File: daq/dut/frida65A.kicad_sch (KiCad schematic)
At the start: 68 parts, among them J1 TP_PWR, J10 TP_LOGIC, J11 TP_OUT, J12 J_P, J16 J_N, J17 Molex_02x04_Mini-Fit_Jr, J2 CONN_IN_P, J3 CONN_IN_N, J4 TP_CFG, J5 CONN_CFG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

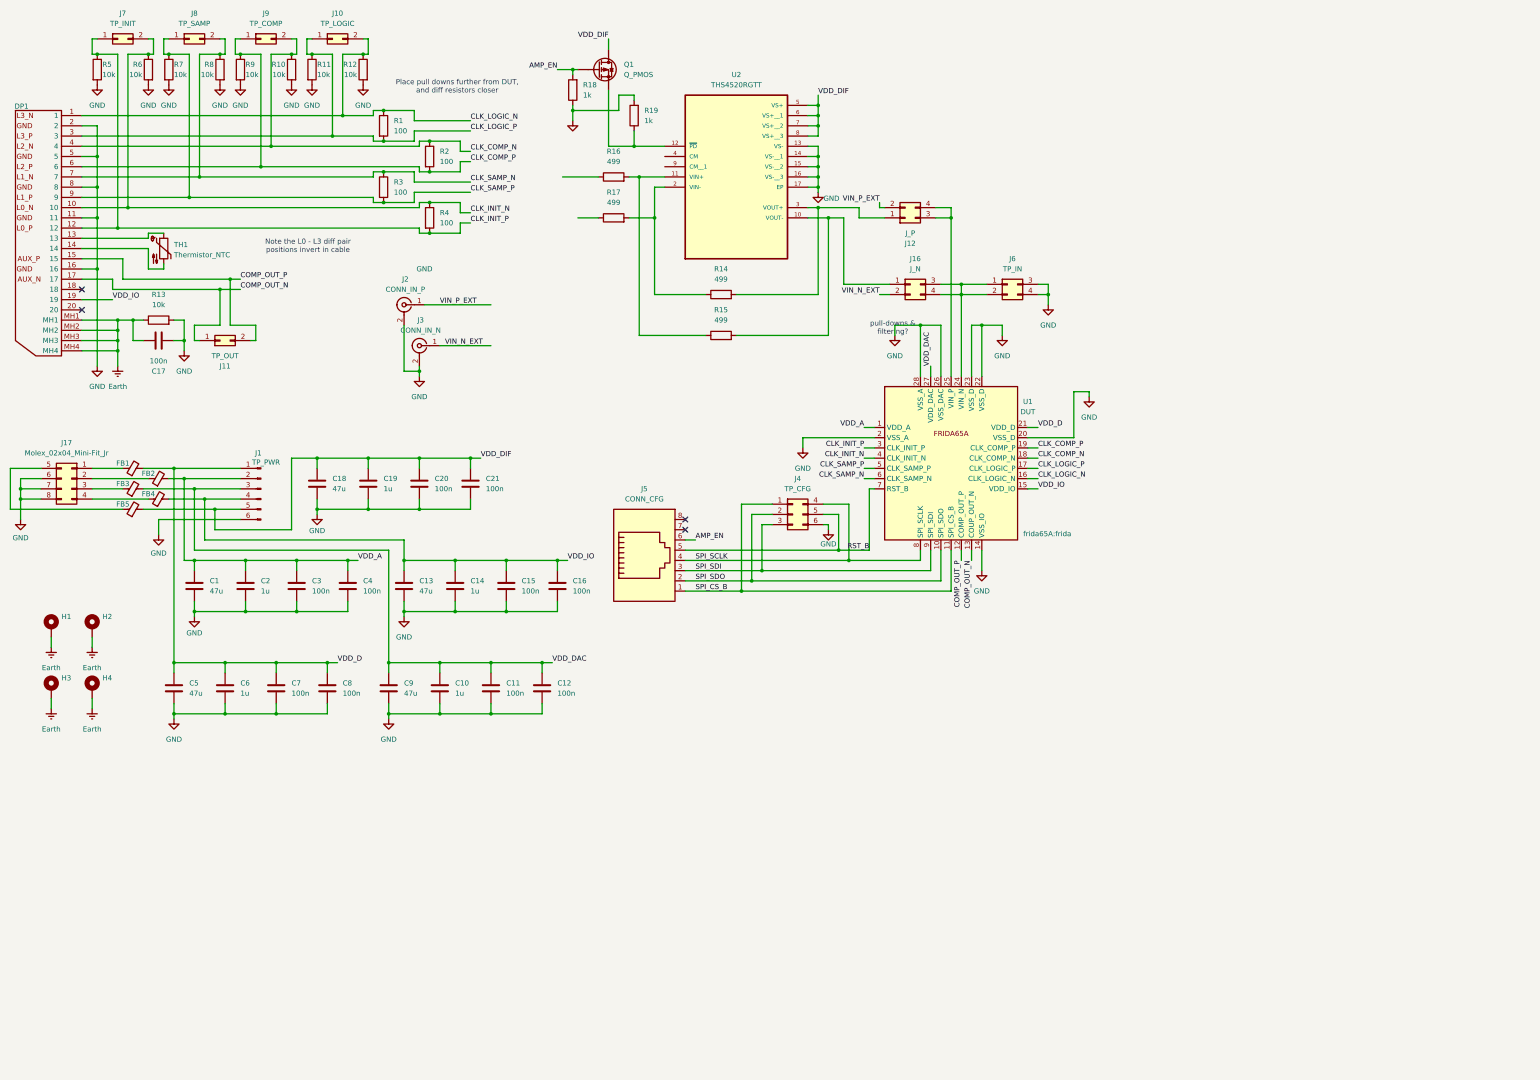
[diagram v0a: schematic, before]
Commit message: Update PCB symbols, footprints, and models. Start work on Spectre simulator montecarlo support.
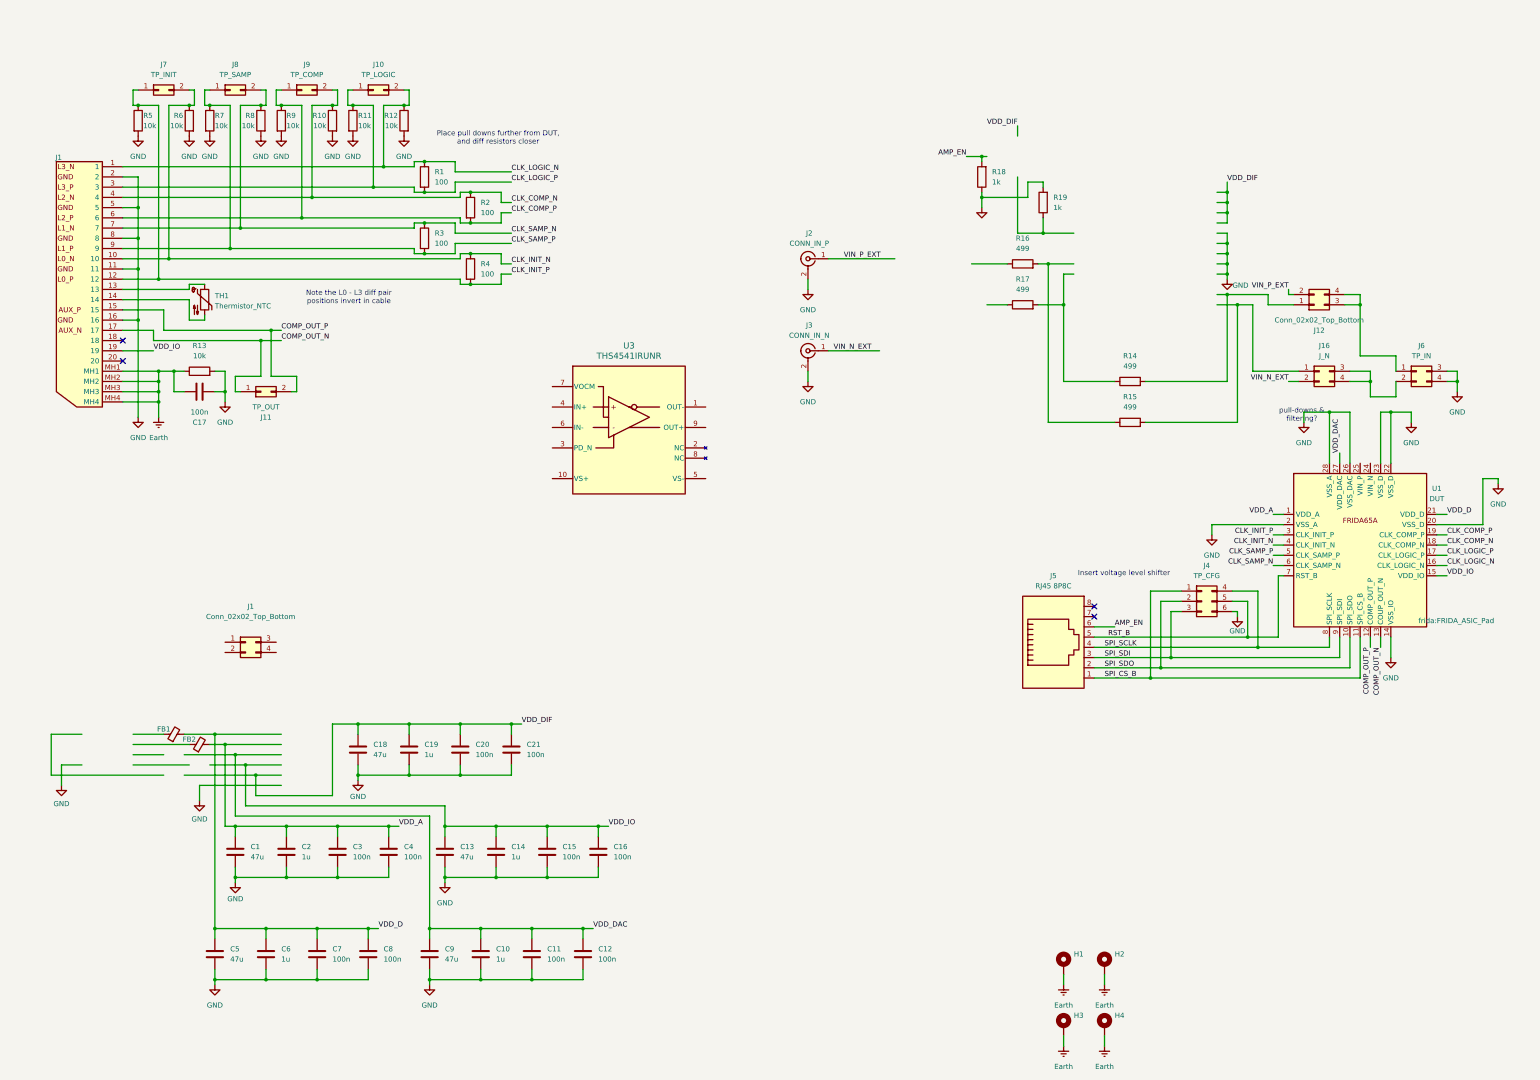
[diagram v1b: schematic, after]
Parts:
- removed DP1: DP, frida65A:displayport, symbol silab:DP Molex 47272-0024
- removed FB3, FB4, FB5: FerriteBead_Small, Resistor_SMD:R_0603_1608Metric, symbol Device:FerriteBead_Small
- removed J1: TP_PWR, frida65A:Molex_Mini-Fit_Jr_5569-08A1_2x04_P4.20mm_Horizontal, symbol Connector:Conn_01x06_Pin
- removed J17: Molex_02x04_Mini-Fit_Jr, Silab:Molex_Mini-Fit_Jr_02x04_horizontal, symbol frida:Molex_02x04_Mini-Fit_Jr
- removed Q1: Q_PMOS, symbol Device:Q_PMOS
- removed U2: THS4520RGTT, frida65A:QFN50P300X300X100-17N, symbol frida:THS4520RGTT
- added J1: Conn_02x02_Top_Bottom, Connector_PinHeader_2.54mm:PinHeader_2x02_P2.54mm_Vertical, symbol Connector_Generic:Conn_02x02_Top_Bottom
- added J1: DP, frida:Molex_DisplayPort_472720024, symbol frida:Molex_DisplayPort_472720024
- added U3: THS4541IRUNR, Package_DFN_QFN:Texas_RUN0010A_WQFN-10_2x2mm_P0.5mm, symbol frida:TI_DiffAmp_THS4541
- J12: value J_P -> Conn_02x02_Top_Bottom; footprint frida65A:Molex_Mini-Fit_Jr_5569-08A1_2x04_P4.20mm_Horizontal -> Connector_PinHeader_2.54mm:PinHeader_2x02_P2.54mm_Vertical
- J16: footprint frida65A:displayport -> frida:Molex_DisplayPort_472720024
- J5: value CONN_CFG -> RJ45 8P8C; footprint Connector_RJ:RJ45_Amphenol_54602-x08_Horizontal -> frida:Molex_RJ45_446200002; symbol frida:RJ45 -> Connector:RJ45
- U1: footprint frida65A:frida -> frida:FRIDA_ASIC_Pad; symbol frida:frida_pad -> frida:FRIDA_ASIC_Pad
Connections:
- net CLK_COMP_N: now also J1.4
- net CLK_COMP_P: now also J1.6
- net CLK_INIT_N: now also J1.10
- net CLK_INIT_P: now also J1.12
- net CLK_LOGIC_N: now also J1.1
- net CLK_LOGIC_P: now also J1.3
- net CLK_SAMP_N: now also J1.7
- net CLK_SAMP_P: now also J1.9
- net COMP_OUT_N: now also J1.17
- net COMP_OUT_P: now also J1.15
- net Earth: now also J1.MH1, J1.MH2, J1.MH3, J1.MH4
- net GND: now also J1.11, J1.16, J1.2, J1.5, J1.8
- net VDD_IO: now also J1.19
- net at J16.3 (Pin_3), J16.4 (Pin_4), J6.2 (Pin_2): no longer J6.1 (Pin_1), U1.24 (VIN_N)
- net at J12.3 (Pin_3), J12.4 (Pin_4): now also J6.1 (Pin_1); no longer U1.25 (VIN_P)
- net at TH1.1: now also J1.13
- net at TH1.2: now also J1.14
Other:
- note added: "Insert voltage level shifter"
- moved on the sheet: C1, C10, C11, C12, C13, C14, C15, C16, C17, C18, C19, C2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

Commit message: Update schematic with new arch, and remove 2.54mm testpoints
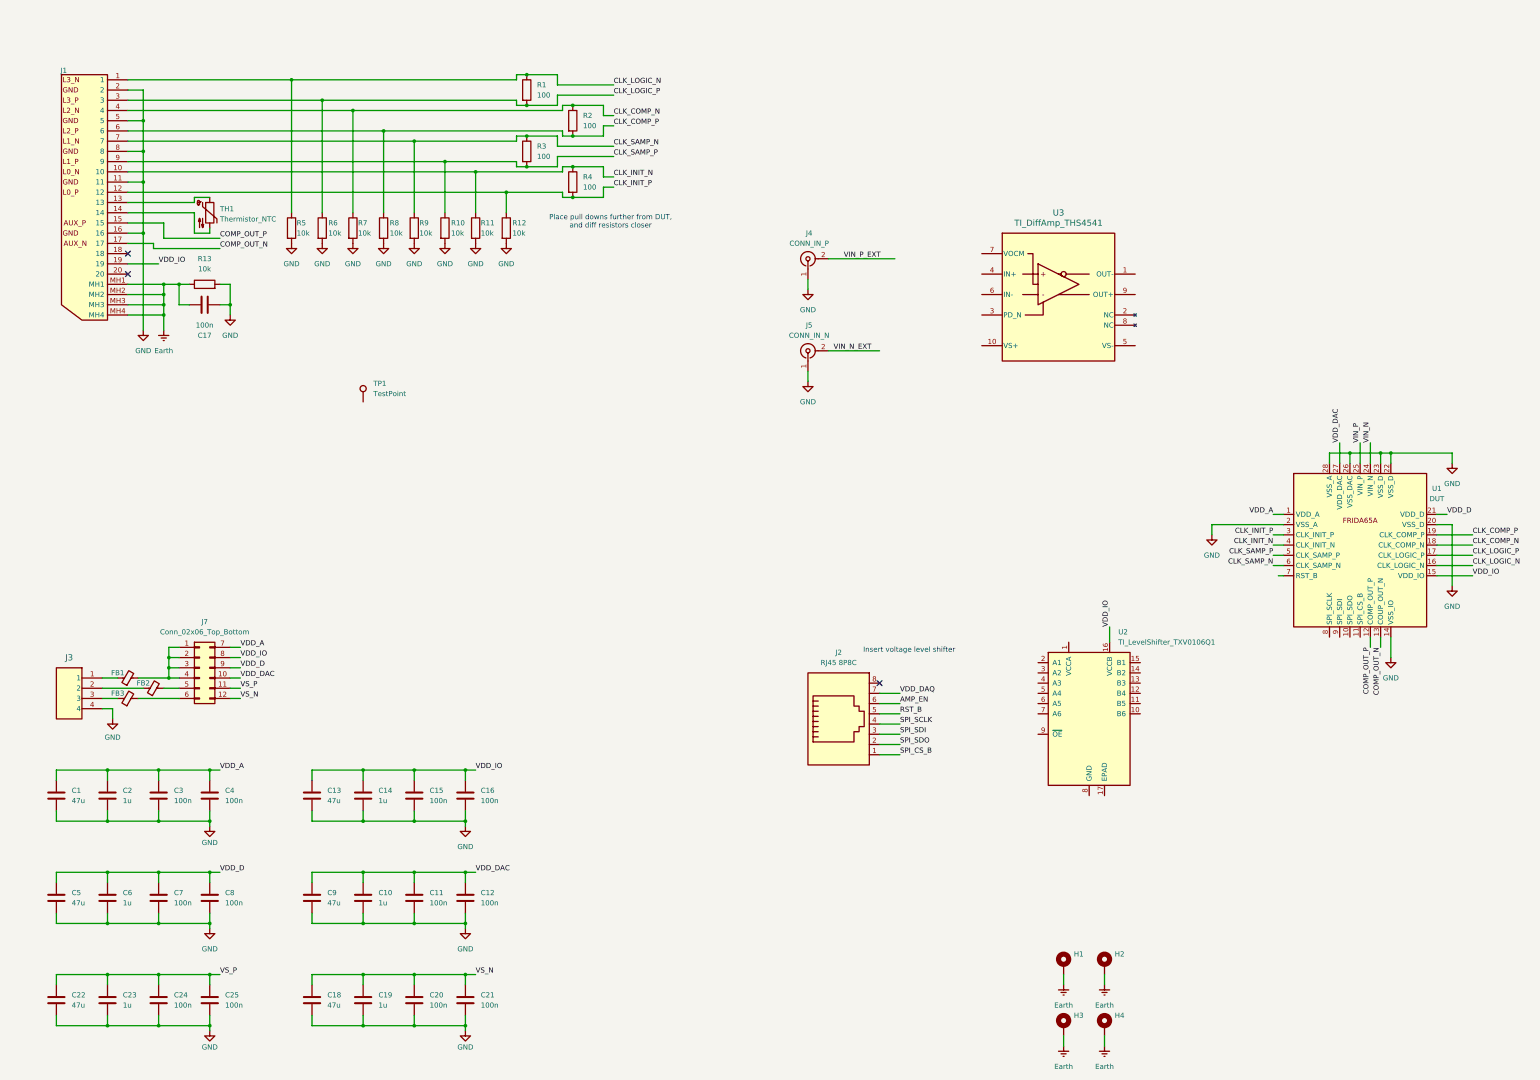
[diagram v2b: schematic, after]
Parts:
- removed J1, J12: Conn_02x02_Top_Bottom, Connector_PinHeader_2.54mm:PinHeader_2x02_P2.54mm_Vertical, symbol Connector_Generic:Conn_02x02_Top_Bottom
- removed J10: TP_LOGIC, Connector_PinHeader_2.54mm:PinHeader_2x01_P2.54mm_Vertical, symbol Connector_Generic:Conn_02x01
- removed J11: TP_OUT, Connector_PinHeader_2.54mm:PinHeader_2x01_P2.54mm_Vertical, symbol Connector_Generic:Conn_02x01
- removed J16: J_N, frida:Molex_DisplayPort_472720024, symbol Connector_Generic:Conn_02x02_Top_Bottom
- removed J4: TP_CFG, Connector_PinHeader_2.54mm:PinHeader_2x03_P2.54mm_Vertical, symbol Connector_Generic:Conn_02x03_Top_Bottom
- removed J6: TP_IN, Connector_PinHeader_2.54mm:PinHeader_2x02_P2.54mm_Vertical, symbol Connector_Generic:Conn_02x02_Top_Bottom
- removed J7: TP_INIT, Connector_PinHeader_2.54mm:PinHeader_2x01_P2.54mm_Vertical, symbol Connector_Generic:Conn_02x01
- removed J8: TP_SAMP, Connector_PinHeader_2.54mm:PinHeader_2x01_P2.54mm_Vertical, symbol Connector_Generic:Conn_02x01
- removed J9: TP_COMP, Connector_PinHeader_2.54mm:PinHeader_2x01_P2.54mm_Vertical, symbol Connector_Generic:Conn_02x01
- removed R14, R15, R16, R17: 499, Resistor_SMD:R_0603_1608Metric, symbol Device:R
- removed R18, R19: 1k, Resistor_SMD:R_0603_1608Metric, symbol Device:R
- added C22: 47u, Capacitor_SMD:C_0603_1608Metric, symbol Device:C
- added C23: 1u, Capacitor_SMD:C_0603_1608Metric, symbol Device:C
- added C24, C25: 100n, Capacitor_SMD:C_0603_1608Metric, symbol Device:C
- added FB3: FerriteBead_Small, Resistor_SMD:R_0603_1608Metric, symbol Device:FerriteBead_Small
- added J3: Molex_MiniFitJr_469990014, frida:Molex_MiniFitJr_469990014, symbol frida:Molex_MiniFitJr_469990014
- added J7: Conn_02x06_Top_Bottom, symbol Connector_Generic:Conn_02x06_Top_Bottom
- added TP1: TestPoint, TestPoint:TestPoint_Pad_D2.0mm, symbol Connector:TestPoint
- added U2: TI_LevelShifter_TXV0106Q1, Package_DFN_QFN:WQFN-16-1EP_4x4mm_P0.5mm_EP2.6x2.6mm, symbol frida:TI_LevelShifter_TXV0106Q1
- J4: renamed from J2; footprint Connector_Coaxial:SMA_Amphenol_901-143_Horizontal -> frida:Molex_SMA_733910070; symbol dmaps_components:Conn_LEMO -> frida:Molex_SMA_733910070
- J5: renamed from J3; footprint Connector_Coaxial:SMA_Amphenol_901-143_Horizontal -> frida:Molex_SMA_733910070; symbol dmaps_components:Conn_LEMO -> frida:Molex_SMA_733910070
- U3: value THS4541IRUNR -> TI_DiffAmp_THS4541; footprint Package_DFN_QFN:Texas_RUN0010A_WQFN-10_2x2mm_P0.5mm -> frida:TI_DiffAmp_THS4541
- renumbered J5 to J2
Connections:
- net CLK_COMP_N: now also R7.1; no longer R10.1
- net CLK_COMP_P: now also R8.1; no longer R9.1
- net CLK_INIT_N: now also R11.1; no longer R6.1
- net CLK_INIT_P: now also R12.1; no longer R5.1
- net CLK_LOGIC_N: now also R5.1; no longer R12.1
- net CLK_LOGIC_P: now also R6.1; no longer R11.1
- net CLK_SAMP_N: now also R9.1; no longer R8.1
- net CLK_SAMP_P: now also R10.1; no longer R7.1
- net GND: now also J4.1 (In), J5.1 (In), C22.2, C23.2, C24.2, C25.2, J3.4; no longer J4.2 (Ext), J5.2 (Ext)
- net RST_B: no longer U1.7 (RST_B)
- net SPI_CS_B: no longer U1.11 (SPI_CS_B)
- net SPI_SCLK: no longer U1.8 (SPI_SCLK)
- net SPI_SDI: no longer U1.9 (SPI_SDI)
- net SPI_SDO: no longer U1.10 (SPI_SDO)
- net VDD_A: now also J7.7 (Pin_7); no longer FB2.2
- net VDD_D: now also J7.9 (Pin_9); no longer FB1.2
- net VDD_DAC: now also J7.10 (Pin_10)
- net VDD_IO: now also J7.8 (Pin_8), U2.16 (VCCB)
- net VIN_N_EXT: now also J5.2 (Ext); no longer J5.1 (In)
- net VIN_P_EXT: now also J4.2 (Ext); no longer J4.1 (In)
- net at FB1.1: now also J3.1
- net VIN_N: now reaches U1.24 (VIN_N)
- net VIN_P: now reaches U1.25 (VIN_P)
- net at FB2.1: now also J3.2
- net VDD_DAQ: now reaches J2.7
- net VDD_DIF renamed VS_N
- net VS_N: now also J7.12 (Pin_12)
- new net: FB1.2, J7.1 (Pin_1), J7.2 (Pin_2), J7.3 (Pin_3), J7.4 (Pin_4)
- new net: FB3.1, J3.3
- new net: FB3.2, J7.6 (Pin_6)
- new net: FB2.2, J7.5 (Pin_5)
- new net VS_P: C22.1, C23.1, C24.1, C25.1, J7.11 (Pin_11)
- no-connect marks 4 -> 3
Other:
- note removed: "Note the L0 - L3 diff pair positions invert in cable"
- note removed: "pull-downs & filtering?"
- moved on the sheet: C1, C10, C11, C12, C13, C14, C15, C16, C17, C18, C19, C2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

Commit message: Update PCB schem connectors and devices, add initial test points
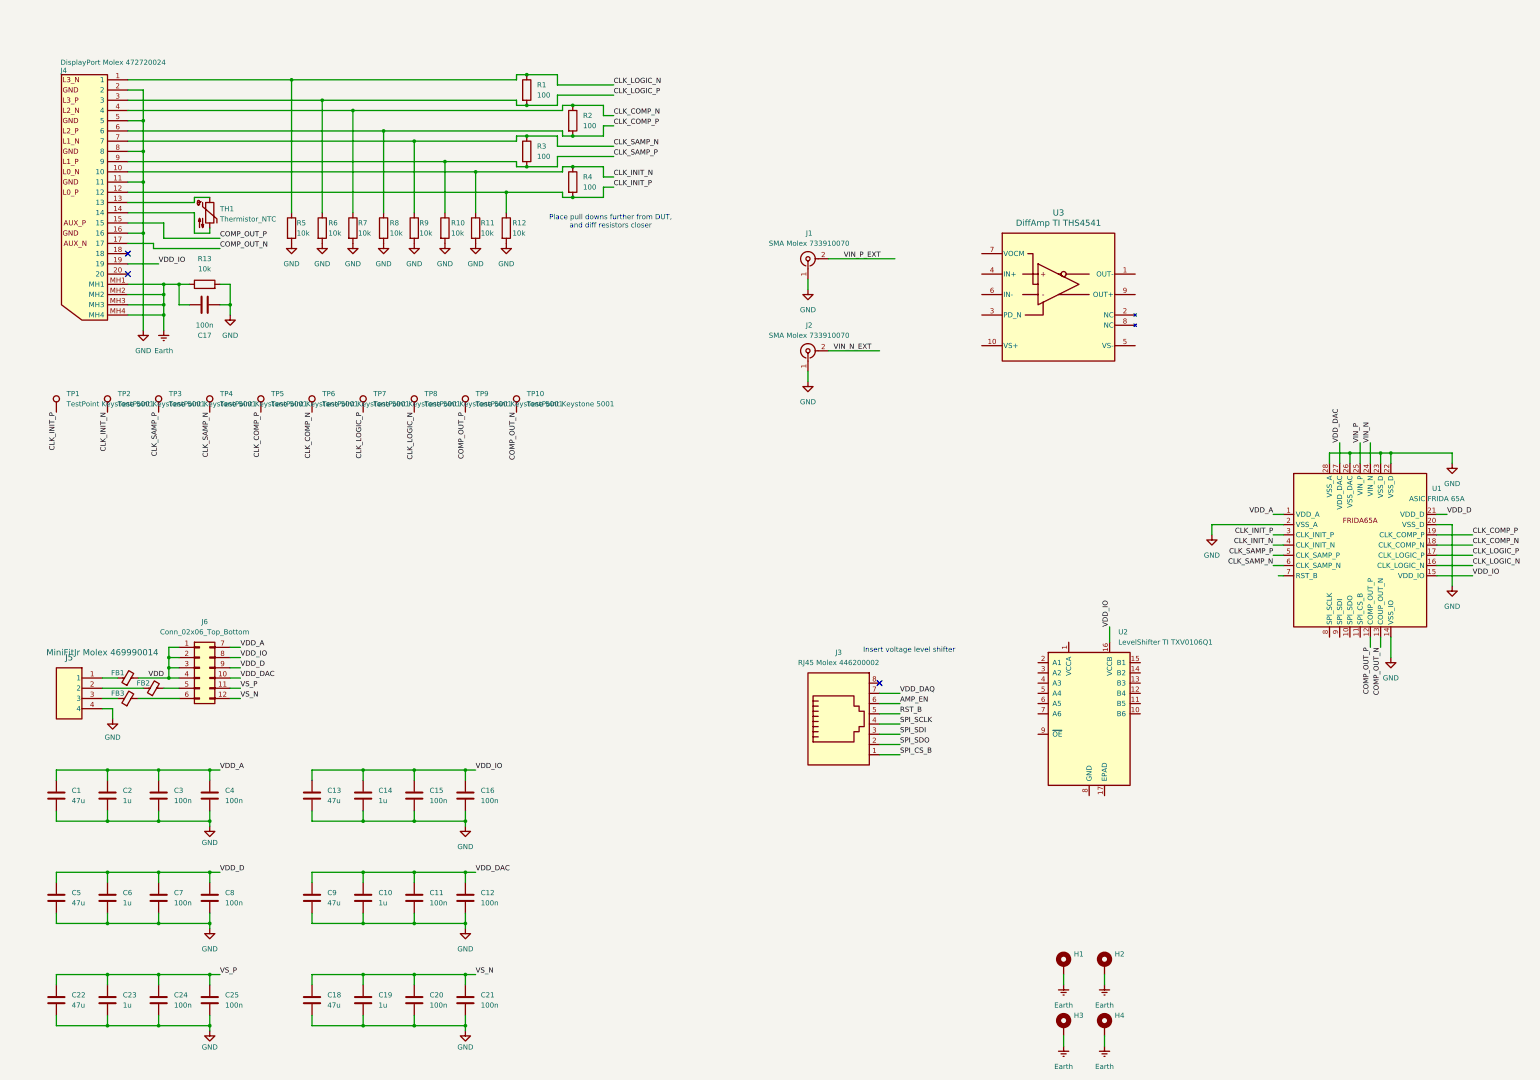
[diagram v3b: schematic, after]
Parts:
- added TP10, TP2, TP3, TP4, TP5, TP6, TP7, TP8, TP9: TestPoint Keystone 5001, TestPoint:TestPoint_Keystone_5000-5004_Miniature, symbol Connector:TestPoint
- J1: renamed from J4; value CONN_IN_P -> SMA Molex 733910070
- J2: renamed from J5; value CONN_IN_N -> SMA Molex 733910070
- J3: renamed from J2; value RJ45 8P8C -> RJ45 Molex 446200002
- J4: renamed from J1; value DP -> DisplayPort Molex 472720024
- J5: renamed from J3; value Molex_MiniFitJr_469990014 -> MiniFitJr Molex 469990014
- TP1: value TestPoint -> TestPoint Keystone 5001; footprint TestPoint:TestPoint_Pad_D2.0mm -> TestPoint:TestPoint_Keystone_5000-5004_Miniature
- U1: value DUT -> ASIC FRIDA 65A
- U2: value TI_LevelShifter_TXV0106Q1 -> LevelShifter TI TXV0106Q1; footprint Package_DFN_QFN:WQFN-16-1EP_4x4mm_P0.5mm_EP2.6x2.6mm -> frida:TI_LevelShifter_TXV0106Q1
- U3: value TI_DiffAmp_THS4541 -> DiffAmp TI THS4541
- renumbered J7 to J6
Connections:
- net CLK_COMP_N: now also TP6.1
- net CLK_COMP_P: now also TP5.1
- net CLK_INIT_N: now also TP2.1
- net CLK_INIT_P: now also TP1.1
- net CLK_LOGIC_N: now also TP8.1
- net CLK_LOGIC_P: now also TP7.1
- net CLK_SAMP_N: now also TP4.1
- net CLK_SAMP_P: now also TP3.1
- net COMP_OUT_N: now also TP10.1
- net COMP_OUT_P: now also TP9.1
- net VDD: now reaches FB1.2, J6.1 (Pin_1), J6.2 (Pin_2), J6.3 (Pin_3), J6.4 (Pin_4)
